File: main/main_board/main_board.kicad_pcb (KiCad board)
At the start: 4 copper layers, 426.7 x 242.2 mm, 139 parts, among them J1 Conn_02x08_Odd_Even, J2 MCLK, J7 SCKB, J8 SCKA, J9 MCLK, M1 microzed, P2 my_pcie_8x, P3 my_pcie_8x, P4 my_pcie_8x, P5 my_pcie_8x, P6 my_pcie_8x, U1 MAX6220ASA-5.0+, U10 74AUP1G74, U11 MCP1755S-3302E/DB, U12 FIN1047, U13 DS90LV048, U14 74LVC541A, U15 FIN1047, U16 FIN1047, U17 FIN1047, U2 OPA209, U3 MCP1755S-3302E/DB, U4 MCP1755S-3302E/DB, U5 DS90LV048, U6 AP3761C-25SP, X2 Si570

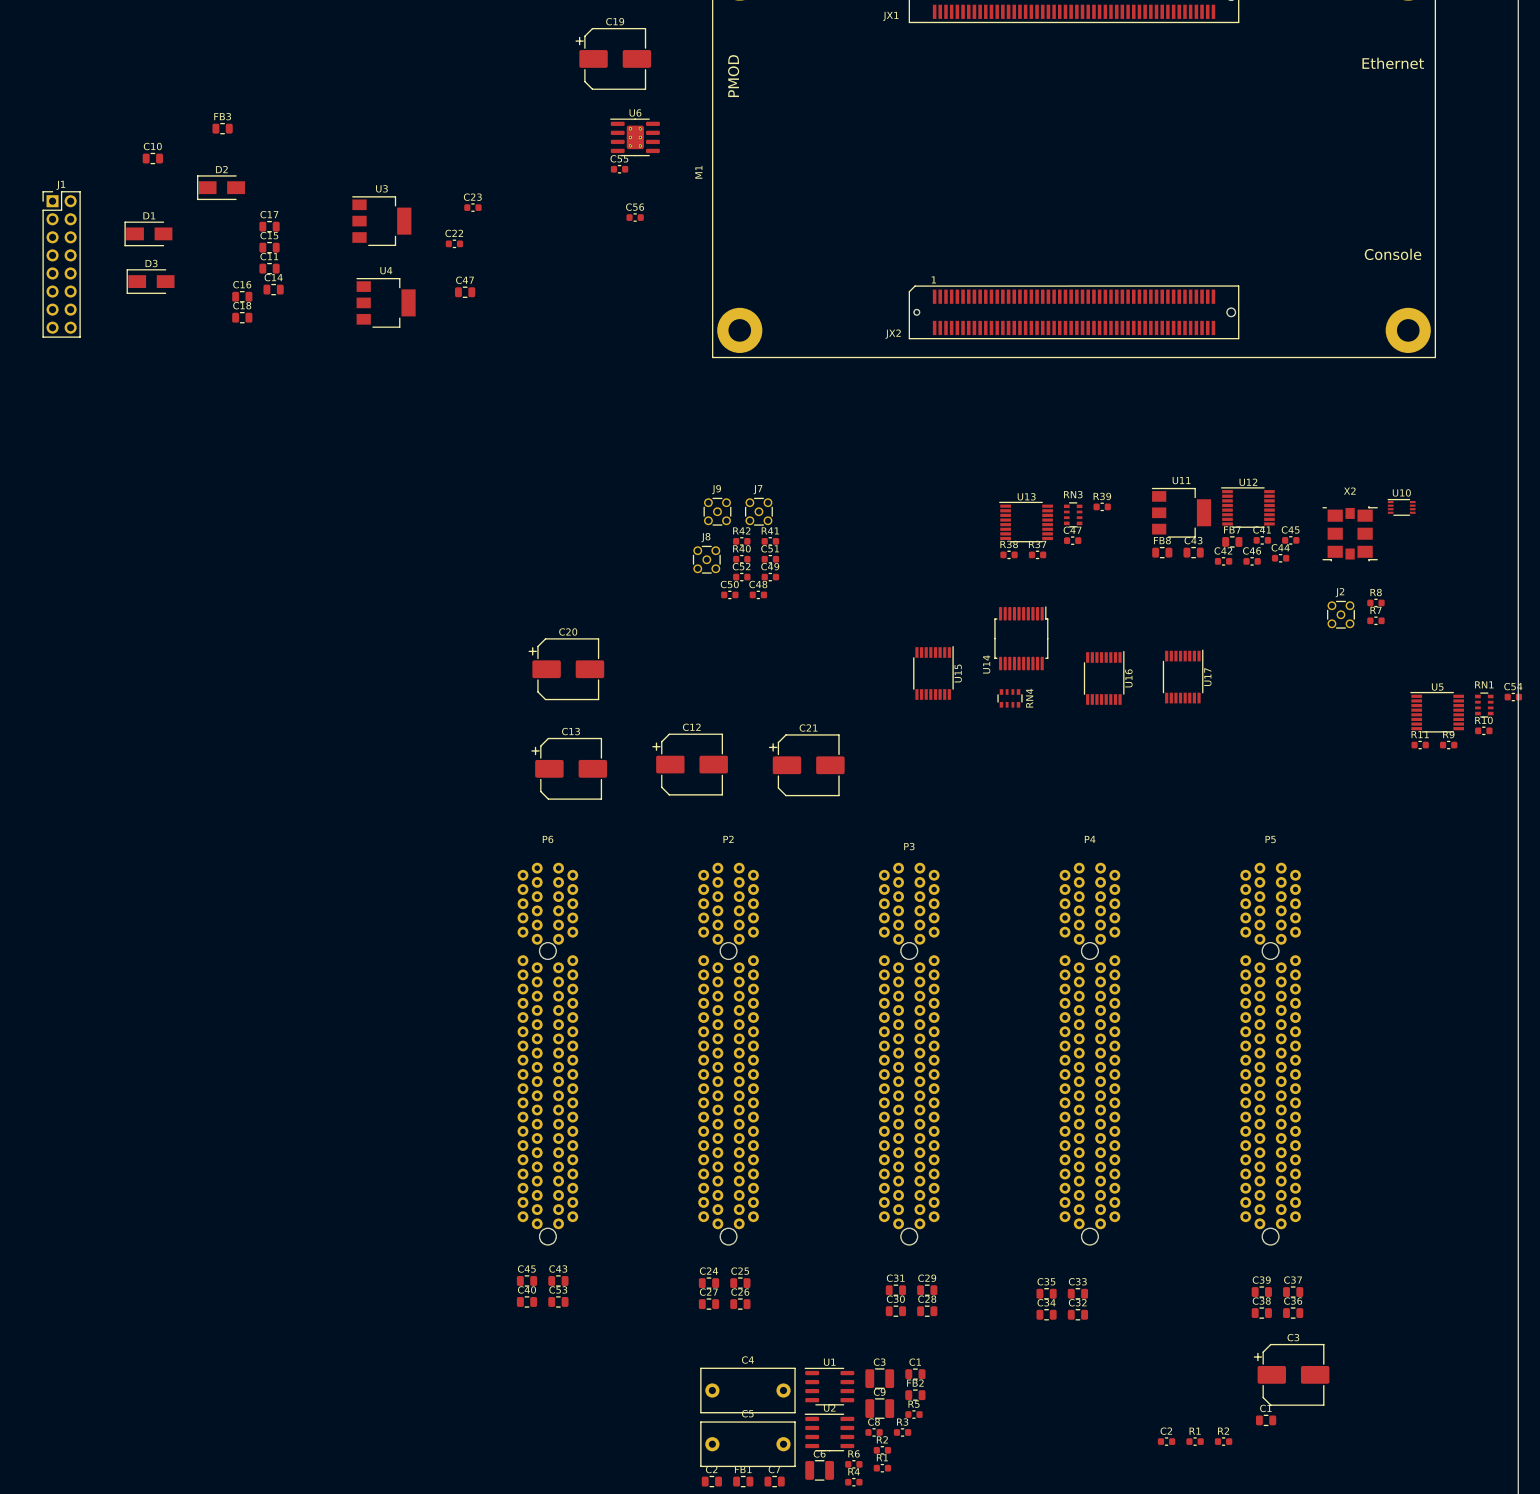
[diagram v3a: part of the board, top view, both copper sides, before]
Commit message: Schematic is mostly complete (except for BIST DACs), and passes ERC.  Rough placement of components on PCB.
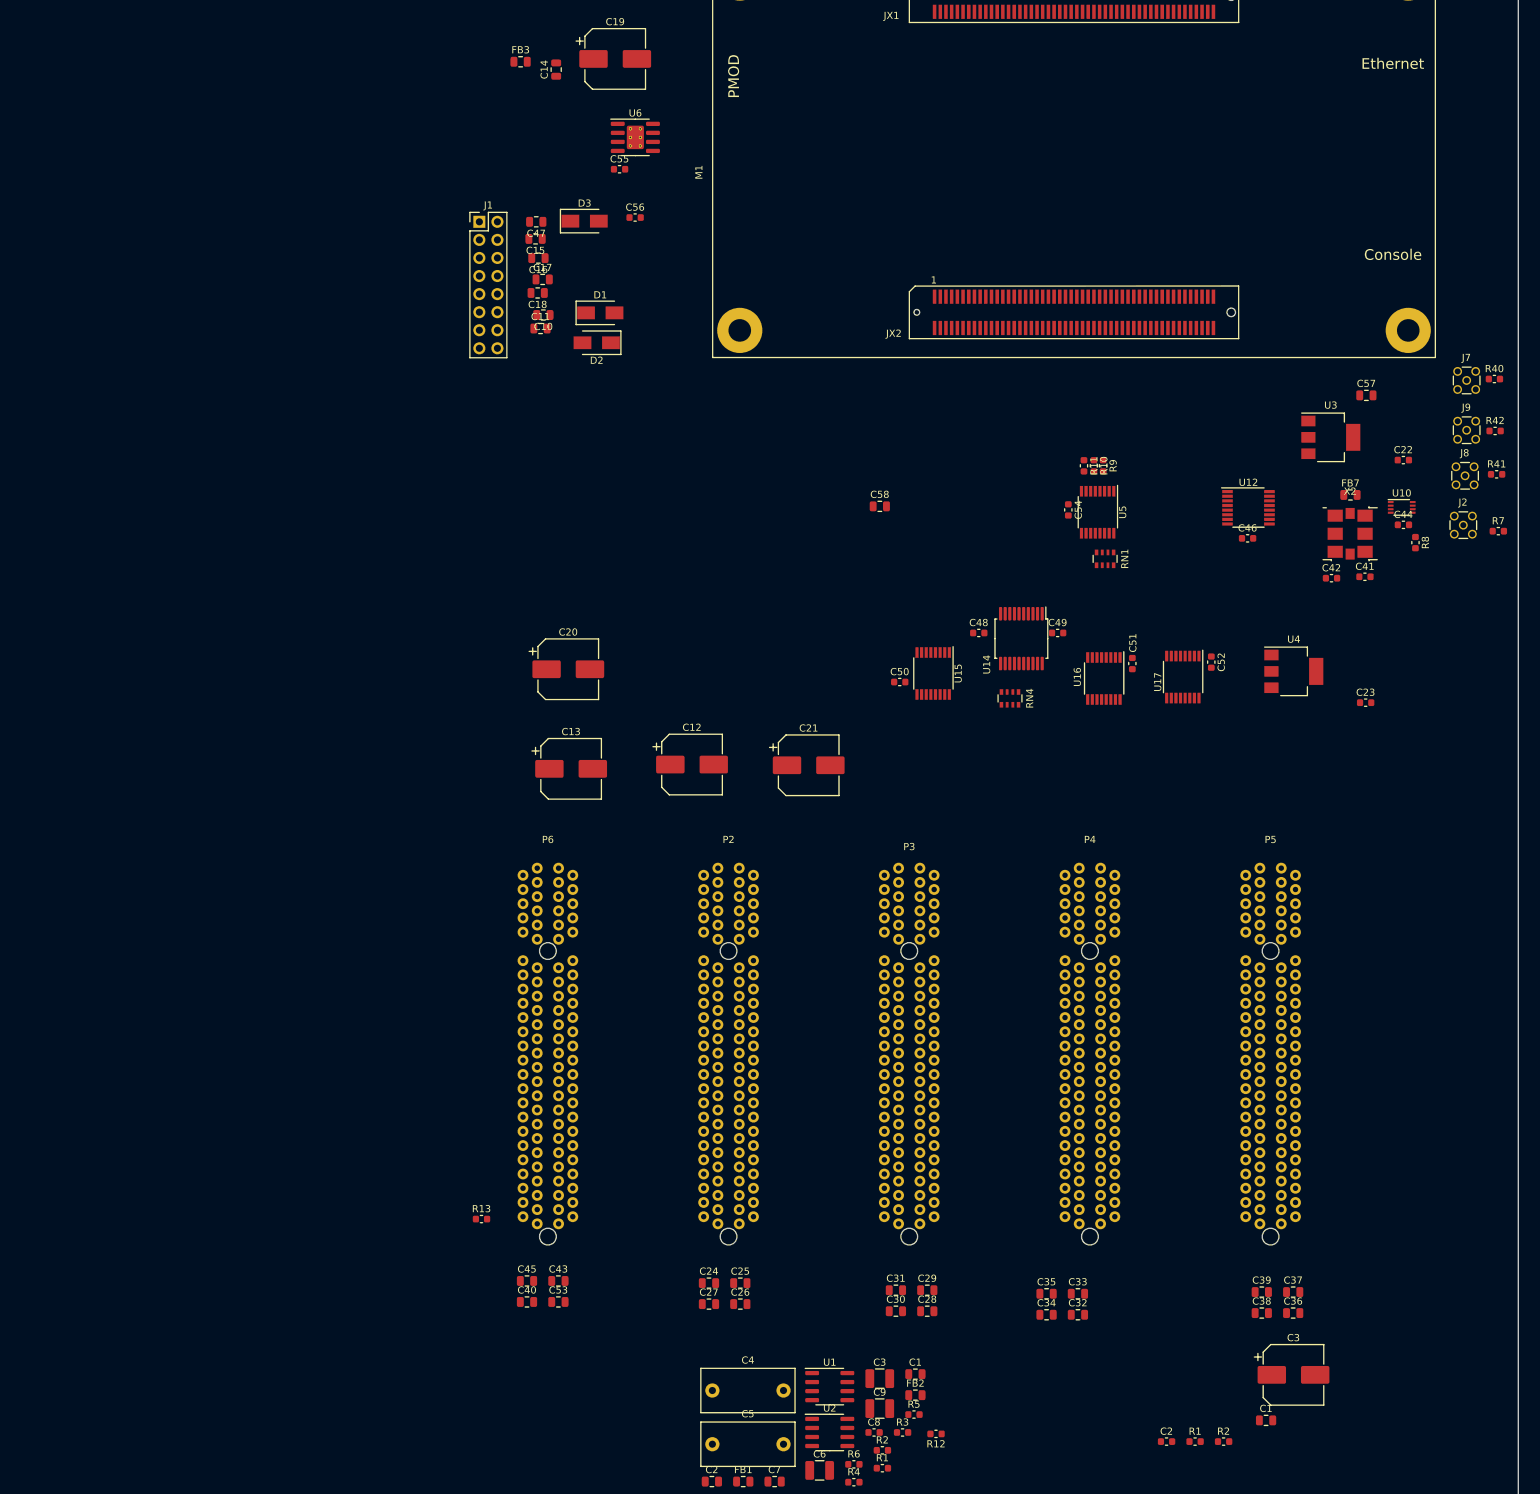
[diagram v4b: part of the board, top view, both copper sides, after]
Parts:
- removed the C43 at (409.0, 121.0)
- removed the C45 at (422.7, 119.3)
- removed the C47 at (392.0, 119.3)
- removed FB8: 21 Ohm, Inductor_SMD:L_0805_2012Metric
- removed R37, R38, R39: 100, Resistor_SMD:R_0603_1608Metric
- removed RN3: 33, Resistor_SMD:R_Array_Convex_4x0603
- removed U11: MCP1755S-3302E/DB, Package_TO_SOT_SMD:SOT-223-3_TabPin2
- removed U13: DS90LV048, Package_SO:TSSOP-16_4.4x5mm_P0.65mm
- added C57: 1uF, Capacitor_SMD:C_0805_2012Metric, F.Cu at (433.3, 98.9)
- added C58: 1uF, Capacitor_SMD:C_0805_2012Metric, F.Cu at (364.9, 114.5)
- added R12: 0, Resistor_SMD:R_0603_1608Metric, F.Cu at (372.8, 244.9)
- added R13: 0, Resistor_SMD:R_0603_1608Metric, F.Cu at (308.9, 214.7)
- moved C23 143.5 mm to (433.2, 142.1)
- moved U4 137.7 mm to (423.1, 137.7)
- moved U3 136.8 mm to (428.3, 104.8)
- moved C22 136.8 mm to (438.5, 108.0)
- moved R40 108.8 mm to (451.3, 96.6)
- moved J8 107.3 mm to (447.2, 110.2)
- moved R42 107.0 mm to (451.4, 103.9)
- moved J9 105.9 mm to (447.4, 103.8)
- moved R41 102.5 mm to (451.6, 110.0)
- moved J7 101.2 mm to (447.4, 96.8)
- moved C54 67.9 mm to (391.4, 115.0), turned to 270 degrees
- moved C52 67.1 mm to (411.5, 136.4), turned to 270 degrees
- moved R10 66.3 mm to (395.0, 108.8), turned to 270 degrees
- moved D1 64.4 mm to (325.6, 87.3)
- moved R9 62.5 mm to (396.3, 108.8), turned to 270 degrees
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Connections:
- C1 pad 1: VREF- -> GND
- C14 pad 1: GNDD -> GND
- C19 pad 2: GNDD -> GND
- C2 pad 1: VREF- -> GND
- C3 pad 2: VREF- -> GND
- C4 pad 2: VREF- -> GND
- C5 pad 2: VREF- -> GND
- C55 pad 2: GNDD -> GND
- C56 pad 2: GNDD -> GND
- C6 pad 2: VREF- -> GND
- C7 pad 1: VREF- -> GND
- C9 pad 2: VREF- -> GND
- M1 pad A015: GNDD -> GND
- M1 pad A016: GNDD -> GND
- M1 pad A021: GNDD -> GND
- M1 pad A022: GNDD -> GND
- M1 pad A027: GNDD -> GND
- M1 pad A028: GNDD -> GND
- M1 pad A033: GNDD -> GND
- M1 pad A034: GNDD -> GND
- M1 pad A039: GNDD -> GND
- M1 pad A040: GNDD -> GND
- M1 pad A045: GNDD -> GND
- M1 pad A046: GNDD -> GND
- M1 pad A051: GNDD -> GND
- M1 pad A052: GNDD -> GND
- M1 pad A065: GNDD -> GND
- M1 pad A066: GNDD -> GND
- M1 pad A071: GNDD -> GND
- M1 pad A072: GNDD -> GND
- M1 pad A077: GNDD -> GND
- M1 pad A085: GNDD -> GND
- M1 pad A086: GNDD -> GND
- M1 pad A095: GNDD -> GND
- M1 pad A096: GNDD -> GND
- M1 pad B015: GNDD -> GND
- M1 pad B016: GNDD -> GND
- M1 pad B021: GNDD -> GND
- M1 pad B022: GNDD -> GND
- M1 pad B027: GNDD -> GND
- M1 pad B028: GNDD -> GND
- M1 pad B033: GNDD -> GND
- M1 pad B034: GNDD -> GND
- M1 pad B039: GNDD -> GND
- M1 pad B040: GNDD -> GND
- M1 pad B045: GNDD -> GND
- M1 pad B046: GNDD -> GND
- M1 pad B051: GNDD -> GND
- M1 pad B052: GNDD -> GND
- M1 pad B065: GNDD -> GND
- M1 pad B066: GNDD -> GND
- M1 pad B071: GNDD -> GND
- M1 pad B072: GNDD -> GND
- M1 pad B077: GNDD -> GND
- M1 pad B085: GNDD -> GND
- M1 pad B086: GNDD -> GND
- M1 pad B091: GNDD -> GND
- M1 pad B092: GNDD -> GND
- P2 pad A29: VREF- -> GND
- P2 pad A30: VREF- -> GND
- P2 pad A31: VREF- -> GND
- P2 pad A32: VREF- -> GND
- P2 pad A33: VREF- -> GND
- P2 pad A34: VREF- -> GND
- P2 pad A35: VREF- -> GND
- P2 pad A41: VREF- -> GND
- P2 pad A44: VREF- -> GND
- P2 pad A47: VREF- -> GND
- P2 pad B29: VREF- -> GND
- P2 pad B30: VREF- -> GND
- P2 pad B31: VREF- -> GND
- P2 pad B32: VREF- -> GND
- P2 pad B33: VREF- -> GND
- P2 pad B34: VREF- -> GND
- P2 pad B35: VREF- -> GND
- P2 pad B41: VREF- -> GND
- P2 pad B42: VREF- -> GND
- P2 pad B43: VREF- -> GND
- P2 pad B44: VREF- -> GND
- P2 pad B47: VREF- -> GND
- P3 pad A29: VREF- -> GND
- P3 pad A30: VREF- -> GND
- P3 pad A31: VREF- -> GND
- P3 pad A32: VREF- -> GND
- P3 pad A33: VREF- -> GND
- P3 pad A34: VREF- -> GND
- P3 pad A35: VREF- -> GND
- P3 pad A41: VREF- -> GND
- P3 pad A44: VREF- -> GND
- P3 pad A47: VREF- -> GND
- P3 pad B29: VREF- -> GND
- P3 pad B30: VREF- -> GND
- P3 pad B31: VREF- -> GND
- P3 pad B32: VREF- -> GND
- P3 pad B33: VREF- -> GND
- P3 pad B34: VREF- -> GND
- P3 pad B35: VREF- -> GND
- P3 pad B41: VREF- -> GND
- P3 pad B42: VREF- -> GND
- P3 pad B43: VREF- -> GND
- P3 pad B44: VREF- -> GND
- P3 pad B47: VREF- -> GND
- P4 pad A29: VREF- -> GND
- P4 pad A30: VREF- -> GND
- P4 pad A31: VREF- -> GND
- P4 pad A32: VREF- -> GND
- P4 pad A33: VREF- -> GND
- P4 pad A34: VREF- -> GND
- P4 pad A35: VREF- -> GND
- P4 pad A41: VREF- -> GND
- P4 pad A44: VREF- -> GND
- P4 pad A47: VREF- -> GND
- P4 pad B29: VREF- -> GND
- P4 pad B30: VREF- -> GND
- P4 pad B31: VREF- -> GND
- P4 pad B32: VREF- -> GND
- P4 pad B33: VREF- -> GND
- P4 pad B34: VREF- -> GND
- P4 pad B35: VREF- -> GND
- P4 pad B41: VREF- -> GND
- P4 pad B42: VREF- -> GND
- P4 pad B43: VREF- -> GND
- P4 pad B44: VREF- -> GND
- P4 pad B47: VREF- -> GND
- P5 pad A29: VREF- -> GND
- P5 pad A30: VREF- -> GND
- P5 pad A31: VREF- -> GND
- P5 pad A32: VREF- -> GND
- P5 pad A33: VREF- -> GND
- P5 pad A34: VREF- -> GND
- P5 pad A35: VREF- -> GND
- P5 pad A41: VREF- -> GND
- P5 pad A44: VREF- -> GND
- P5 pad A47: VREF- -> GND
- P5 pad B29: VREF- -> GND
- P5 pad B30: VREF- -> GND
- P5 pad B31: VREF- -> GND
- P5 pad B32: VREF- -> GND
- P5 pad B33: VREF- -> GND
- P5 pad B34: VREF- -> GND
- P5 pad B35: VREF- -> GND
- P5 pad B41: VREF- -> GND
- P5 pad B42: VREF- -> GND
- P5 pad B43: VREF- -> GND
- P5 pad B44: VREF- -> GND
- P5 pad B47: VREF- -> GND
- P6 pad A29: VREF- -> GND
- P6 pad A32: VREF- -> GND
- P6 pad A33: VREF- -> GND
- P6 pad A36: VREF- -> GND
- P6 pad A37: VREF- -> GND
- P6 pad A38: VREF- -> GND
- P6 pad A39: VREF- -> GND
- P6 pad A40: VREF- -> GND
- P6 pad A44: VREF- -> GND
- P6 pad A47: VREF- -> GND
- P6 pad B30: VREF- -> GND
- P6 pad B31: VREF- -> GND
- P6 pad B34: VREF- -> GND
- P6 pad B35: VREF- -> GND
- P6 pad B38: VREF- -> GND
- P6 pad B39: VREF- -> GND
- P6 pad B40: VREF- -> GND
- P6 pad B44: VREF- -> GND
- P6 pad B45: VREF- -> GND
- P6 pad B46: VREF- -> GND
- P6 pad B47: VREF- -> GND
- RN4 pad 5: /input_slots/card_slot3/SYNC -> /input_slots/card_slot0/SYNC
- RN4 pad 6: /input_slots/card_slot2/SYNC -> /input_slots/card_slot1/SYNC
- RN4 pad 7: /input_slots/card_slot1/SYNC -> /input_slots/card_slot2/SYNC
- RN4 pad 8: /input_slots/card_slot0/SYNC -> /input_slots/card_slot3/SYNC
- U1 pad 4: VREF- -> GND
- U15 pad 10: /input_slots/card_slot3/SCKA+ -> /input_slots/card_slot0/SCKA+
- U15 pad 11: /input_slots/card_slot2/SCKA+ -> /input_slots/card_slot1/SCKA+
- U15 pad 12: /input_slots/card_slot2/SCKA- -> /input_slots/card_slot1/SCKA-
- U15 pad 13: /input_slots/card_slot1/SCKA- -> /input_slots/card_slot2/SCKA-
- U15 pad 14: /input_slots/card_slot1/SCKA+ -> /input_slots/card_slot2/SCKA+
- U15 pad 15: /input_slots/card_slot0/SCKA+ -> /input_slots/card_slot3/SCKA+
- U15 pad 16: /input_slots/card_slot0/SCKA- -> /input_slots/card_slot3/SCKA-
- U15 pad 9: /input_slots/card_slot3/SCKA- -> /input_slots/card_slot0/SCKA-
- U16 pad 10: /input_slots/card_slot3/SCKB+ -> /input_slots/card_slot0/SCKB+
- U16 pad 11: /input_slots/card_slot2/SCKB+ -> /input_slots/card_slot1/SCKB+
- U16 pad 12: /input_slots/card_slot2/SCKB- -> /input_slots/card_slot1/SCKB-
- U16 pad 13: /input_slots/card_slot1/SCKB- -> /input_slots/card_slot2/SCKB-
- U16 pad 14: /input_slots/card_slot1/SCKB+ -> /input_slots/card_slot2/SCKB+
- U16 pad 15: /input_slots/card_slot0/SCKB+ -> /input_slots/card_slot3/SCKB+
- U16 pad 16: /input_slots/card_slot0/SCKB- -> /input_slots/card_slot3/SCKB-
- U16 pad 9: /input_slots/card_slot3/SCKB- -> /input_slots/card_slot0/SCKB-
- U17 pad 10: /input_slots/card_slot3/MCLK+ -> /input_slots/card_slot0/MCLK+
- U17 pad 11: /input_slots/card_slot2/MCLK+ -> /input_slots/card_slot1/MCLK+
- U17 pad 12: /input_slots/card_slot2/MCLK- -> /input_slots/card_slot1/MCLK-
- U17 pad 13: /input_slots/card_slot1/MCLK- -> /input_slots/card_slot2/MCLK-
- U17 pad 14: /input_slots/card_slot1/MCLK+ -> /input_slots/card_slot2/MCLK+
- U17 pad 15: /input_slots/card_slot0/MCLK+ -> /input_slots/card_slot3/MCLK+
- U17 pad 16: /input_slots/card_slot0/MCLK- -> /input_slots/card_slot3/MCLK-
- U17 pad 9: /input_slots/card_slot3/MCLK- -> /input_slots/card_slot0/MCLK-
- U6 pad 4: GNDD -> GND
- U6 pad 9: GNDD -> GND

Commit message: Mechanical feature layout on main board (edge connector and mount hole locations).  Added some dimension callouts to the input board. Tweaked grounding on main board schematic.  Chassis ground is not connected to main board ground except via an optional capacitor.  Chassis ground comes in on the power connector. Added BIST DAC, including additions to power.sch and input_slots.sch.
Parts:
- removed R13: 0, Resistor_SMD:R_0603_1608Metric
- removed the REF** at (119.4, 279.4)
- removed the REF** at (139.7, 279.4)
- removed the REF** at (180.3, 279.4)
- removed the REF** at (281.9, 279.4)
- removed the REF** at (160.0, 279.4)
- removed the REF** at (302.3, 279.4)
- removed the REF** at (322.6, 279.4)
- removed the REF** at (342.9, 279.4)
- removed the REF** at (363.2, 279.4)
- removed the REF** at (383.5, 279.4)
- removed the REF** at (403.9, 279.4)
- removed the REF** at (78.7, 279.4)
- removed the REF** at (424.2, 279.4)
- removed the REF** at (444.5, 279.4)
- removed the REF** at (99.1, 279.4)
- removed the REF** at (38.1, 279.4)
- removed the REF** at (58.4, 279.4)
- removed the REF** at (261.6, 279.4)
- removed the REF** at (200.7, 279.4)
- removed the REF** at (221.0, 279.4)
- removed the REF** at (241.3, 279.4)
- added C59: 1uF, Capacitor_SMD:C_0805_2012Metric, F.Cu at (109.8, 267.2)
- added C60: 10uF, Capacitor_SMD:C_0603_1608Metric, F.Cu at (120.8, 268.3)
- added C61: 200 pF, Capacitor_SMD:C_0603_1608Metric, F.Cu at (136.1, 267.9)
- added C62: 200 pF, Capacitor_SMD:C_0603_1608Metric, F.Cu at (132.8, 268.3)
- added C63: 1uF, Capacitor_SMD:C_0805_2012Metric, F.Cu at (119.0, 268.1)
- added C64: 200 pF, Capacitor_SMD:C_0603_1608Metric, F.Cu at (133.8, 260.0)
- added C65: 200 pF, Capacitor_SMD:C_0603_1608Metric, F.Cu at (137.0, 259.9)
- added C66: OPT, Capacitor_SMD:C_0603_1608Metric, F.Cu at (118.5, 235.0)
- added FB4: 2K Ohm, Inductor_SMD:L_0805_2012Metric, F.Cu at (135.3, 271.5)
- added FB5: 2K Ohm, Inductor_SMD:L_0805_2012Metric, F.Cu at (133.0, 271.5)
- added FB6: 2K Ohm, Inductor_SMD:L_0805_2012Metric, F.Cu at (133.8, 263.3)
- added FB8: 2K Ohm, Inductor_SMD:L_0805_2012Metric, F.Cu at (137.0, 263.3)
- added R14: 4.99K, Resistor_SMD:R_0603_1608Metric, F.Cu at (137.3, 271.5)
- added R15: 4.99K, Resistor_SMD:R_0603_1608Metric, F.Cu at (130.6, 271.5)
- added R16: 4.99K, Resistor_SMD:R_0603_1608Metric, F.Cu at (140.3, 263.3)
- added R17: 4.99K, Resistor_SMD:R_0603_1608Metric, F.Cu at (130.7, 263.3)
- added REF**: MountingHole_2.7mm_M2.5_ISO7380, main_board:MountingHole_2.7mm_M2.5_ISO7380, F.Cu at (226.1, 31.0)
- added REF**: MountingHole_2.7mm_M2.5_ISO7380, main_board:MountingHole_2.7mm_M2.5_ISO7380, F.Cu at (134.6, 164.3)
- added REF**: MountingHole_2.7mm_M2.5_ISO7380, main_board:MountingHole_2.7mm_M2.5_ISO7380, F.Cu at (104.1, 164.3)
- added REF**: MountingHole_2.7mm_M2.5_ISO7380, main_board:MountingHole_2.7mm_M2.5_ISO7380, F.Cu at (73.7, 164.3)
- added REF**: MountingHole_2.7mm_M2.5_ISO7380, main_board:MountingHole_2.7mm_M2.5_ISO7380, F.Cu at (226.1, 286.8)
- added REF**: MountingHole_2.7mm_M2.5_ISO7380, main_board:MountingHole_2.7mm_M2.5_ISO7380, F.Cu at (195.6, 286.8)
- added REF**: MountingHole_2.7mm_M2.5_ISO7380, main_board:MountingHole_2.7mm_M2.5_ISO7380, F.Cu at (165.1, 286.8)
- added REF**: MountingHole_2.7mm_M2.5_ISO7380, main_board:MountingHole_2.7mm_M2.5_ISO7380, F.Cu at (134.6, 286.8)
- added REF**: MountingHole_2.7mm_M2.5_ISO7380, main_board:MountingHole_2.7mm_M2.5_ISO7380, F.Cu at (104.1, 286.8)
- added REF**: MountingHole_2.7mm_M2.5_ISO7380, main_board:MountingHole_2.7mm_M2.5_ISO7380, F.Cu at (73.7, 286.8)
- added REF**: MountingHole_2.7mm_M2.5_ISO7380, main_board:MountingHole_2.7mm_M2.5_ISO7380, F.Cu at (226.1, 153.5)
- added REF**: MountingHole_2.7mm_M2.5_ISO7380, main_board:MountingHole_2.7mm_M2.5_ISO7380, F.Cu at (195.6, 31.0)
- added REF**: MountingHole_2.7mm_M2.5_ISO7380, main_board:MountingHole_2.7mm_M2.5_ISO7380, F.Cu at (195.6, 153.5)
- added REF**: MountingHole_2.7mm_M2.5_ISO7380, main_board:MountingHole_2.7mm_M2.5_ISO7380, F.Cu at (165.1, 153.5)
- added REF**: MountingHole_2.7mm_M2.5_ISO7380, main_board:MountingHole_2.7mm_M2.5_ISO7380, F.Cu at (134.6, 153.5)
- added REF**: MountingHole_2.7mm_M2.5_ISO7380, main_board:MountingHole_2.7mm_M2.5_ISO7380, F.Cu at (104.1, 153.5)
- added REF**: MountingHole_2.7mm_M2.5_ISO7380, main_board:MountingHole_2.7mm_M2.5_ISO7380, F.Cu at (73.7, 153.5)
- added REF**: MountingHole_2.7mm_M2.5_ISO7380, main_board:MountingHole_2.7mm_M2.5_ISO7380, F.Cu at (43.2, 286.8)
- added REF**: MountingHole_2.7mm_M2.5_ISO7380, main_board:MountingHole_2.7mm_M2.5_ISO7380, F.Cu at (43.2, 164.3)
- added REF**: MountingHole_2.7mm_M2.5_ISO7380, main_board:MountingHole_2.7mm_M2.5_ISO7380, F.Cu at (43.2, 31.0)
- added REF**: MountingHole_2.7mm_M2.5_ISO7380, main_board:MountingHole_2.7mm_M2.5_ISO7380, F.Cu at (43.2, 153.5)
- added REF**: MountingHole_2.7mm_M2.5_ISO7380, main_board:MountingHole_2.7mm_M2.5_ISO7380, F.Cu at (0.00, 286.8)
- added REF**: MountingHole_2.7mm_M2.5_ISO7380, main_board:MountingHole_2.7mm_M2.5_ISO7380, F.Cu at (165.1, 31.0)
- added REF**: MountingHole_2.7mm_M2.5_ISO7380, main_board:MountingHole_2.7mm_M2.5_ISO7380, F.Cu at (0.00, 164.3)
- added REF**: MountingHole_2.7mm_M2.5_ISO7380, main_board:MountingHole_2.7mm_M2.5_ISO7380, F.Cu at (0.00, 153.5)
- added REF**: MountingHole_2.7mm_M2.5_ISO7380, main_board:MountingHole_2.7mm_M2.5_ISO7380, F.Cu at (0.00, 31.0)
- added REF**: MountingHole_2.7mm_M2.5_ISO7380, main_board:MountingHole_2.7mm_M2.5_ISO7380, F.Cu at (134.6, 31.0)
- added REF**: MountingHole_2.7mm_M2.5_ISO7380, main_board:MountingHole_2.7mm_M2.5_ISO7380, F.Cu at (104.1, 31.0)
- added REF**: MountingHole_2.7mm_M2.5_ISO7380, main_board:MountingHole_2.7mm_M2.5_ISO7380, F.Cu at (73.7, 31.0)
- added REF**: MountingHole_2.7mm_M2.5_ISO7380, main_board:MountingHole_2.7mm_M2.5_ISO7380, F.Cu at (226.1, 164.3)
- added REF**: MountingHole_2.7mm_M2.5_ISO7380, main_board:MountingHole_2.7mm_M2.5_ISO7380, F.Cu at (195.6, 164.3)
- added REF**: MountingHole_2.7mm_M2.5_ISO7380, main_board:MountingHole_2.7mm_M2.5_ISO7380, F.Cu at (165.1, 164.3)
- added RN2: 33, Resistor_SMD:R_Array_Convex_4x0603, F.Cu at (131.7, 120.6)
- added U7: MCP1755S-5002E/DB, Package_TO_SOT_SMD:SOT-223-3_TabPin2, F.Cu at (112.3, 260.5)
- added U8: DAC80004IPW, Package_SO:SSOP-14_5.3x6.2mm_P0.65mm, F.Cu at (121.5, 261.2)
- moved C23 261.6 mm to (171.6, 144.6)
- moved C50 261.6 mm to (106.1, 141.7)
- moved C51 261.6 mm to (138.8, 139.1)
- moved U15 261.6 mm to (110.8, 140.5)
- moved U16 261.6 mm to (134.8, 141.2)
- moved U17 261.6 mm to (145.9, 141.0)
- moved U4 261.6 mm to (161.5, 140.2)
- moved C20 259.7 mm to (62.0, 119.6)
- moved C12 259.7 mm to (79.4, 133.0)
- moved C13 259.7 mm to (62.4, 133.6)
- moved C21 259.7 mm to (95.8, 133.1)
- moved C10 259.3 mm to (58.5, 97.8)
- moved C18 259.3 mm to (57.7, 94.7)
- moved C22 259.3 mm to (179.4, 118.2)
- moved C41 259.3 mm to (174.0, 134.6)
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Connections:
- net BIST++_IN renamed BIST++
- net BIST+-_IN renamed BIST+-
- net BIST-+_IN renamed BIST-+
- net BIST--_IN renamed BIST--
- J1 pad 15: GND -> Earth
- J1 pad 16: Net-(J1-Pad16) -> Earth
- M1 pad B069: (no net) -> Net-(M1-PadB069)
- M1 pad B081: FPGA_SYSCLK+ -> Net-(M1-PadB081)
- M1 pad B082: (no net) -> FPGA_SYSCLK+
- M1 pad B083: FPGA_SYSCLK- -> Net-(M1-PadB083)
- M1 pad B084: (no net) -> FPGA_SYSCLK-
- R10 pad 1: Net-(M1-PadB073) -> Net-(M1-PadB074)
- R10 pad 2: Net-(M1-PadB075) -> Net-(M1-PadB076)
- R11 pad 1: Net-(M1-PadB074) -> Net-(M1-PadB081)
- R11 pad 2: Net-(M1-PadB076) -> Net-(M1-PadB083)
- R9 pad 1: Net-(M1-PadB068) -> Net-(M1-PadB073)
- R9 pad 2: Net-(M1-PadB070) -> Net-(M1-PadB075)
- U14 pad 11: Net-(RN4-Pad4) -> Net-(RN2-Pad4)
- U14 pad 12: Net-(RN4-Pad3) -> Net-(RN2-Pad3)
- U14 pad 13: Net-(RN4-Pad2) -> Net-(RN2-Pad2)
- U14 pad 14: Net-(RN4-Pad1) -> Net-(RN2-Pad1)
- U14 pad 15: Net-(U14-Pad15) -> Net-(RN4-Pad4)
- U14 pad 16: Net-(U14-Pad16) -> Net-(RN4-Pad3)
- U14 pad 17: Net-(U14-Pad17) -> Net-(RN4-Pad2)
- U14 pad 18: Net-(U14-Pad18) -> Net-(RN4-Pad1)
- U14 pad 2: Net-(U14-Pad2) -> Net-(M1-PadB070)
- U14 pad 3: Net-(U14-Pad3) -> Net-(M1-PadB070)
- U14 pad 4: Net-(U14-Pad4) -> Net-(M1-PadB070)
- U14 pad 5: Net-(U14-Pad5) -> Net-(M1-PadB070)
- U14 pad 7: Net-(M1-PadB067) -> Net-(M1-PadB069)
- U14 pad 8: Net-(M1-PadB067) -> Net-(M1-PadB068)
- U14 pad 9: Net-(M1-PadB067) -> GND
- U5 pad 3: Net-(M1-PadB068) -> Net-(M1-PadB073)
- U5 pad 4: Net-(M1-PadB070) -> Net-(M1-PadB075)
- U5 pad 5: Net-(M1-PadB075) -> Net-(M1-PadB076)
- U5 pad 6: Net-(M1-PadB073) -> Net-(M1-PadB074)
- U5 pad 7: Net-(M1-PadB074) -> Net-(M1-PadB081)
- U5 pad 8: Net-(M1-PadB076) -> Net-(M1-PadB083)
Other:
- board size 426.7 x 242.2 mm -> 208.3 x 261.9 mm
- board text added: "42 HP (half rack)"
- board text added: "Bottom plugin card edge"
- board text added: "Enclosure right side"
- board text added: "Pitch line at at enclosure divider"
- board text added: "Top plugin card edge"
